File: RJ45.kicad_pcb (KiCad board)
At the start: 2 copper layers, 19.1 x 34.9 mm, 3 parts, among them J1 Conn_01x06, J2 RJ45_Amphenol_RJMG1BD3B8K1ANR, J3 Conn_01x06

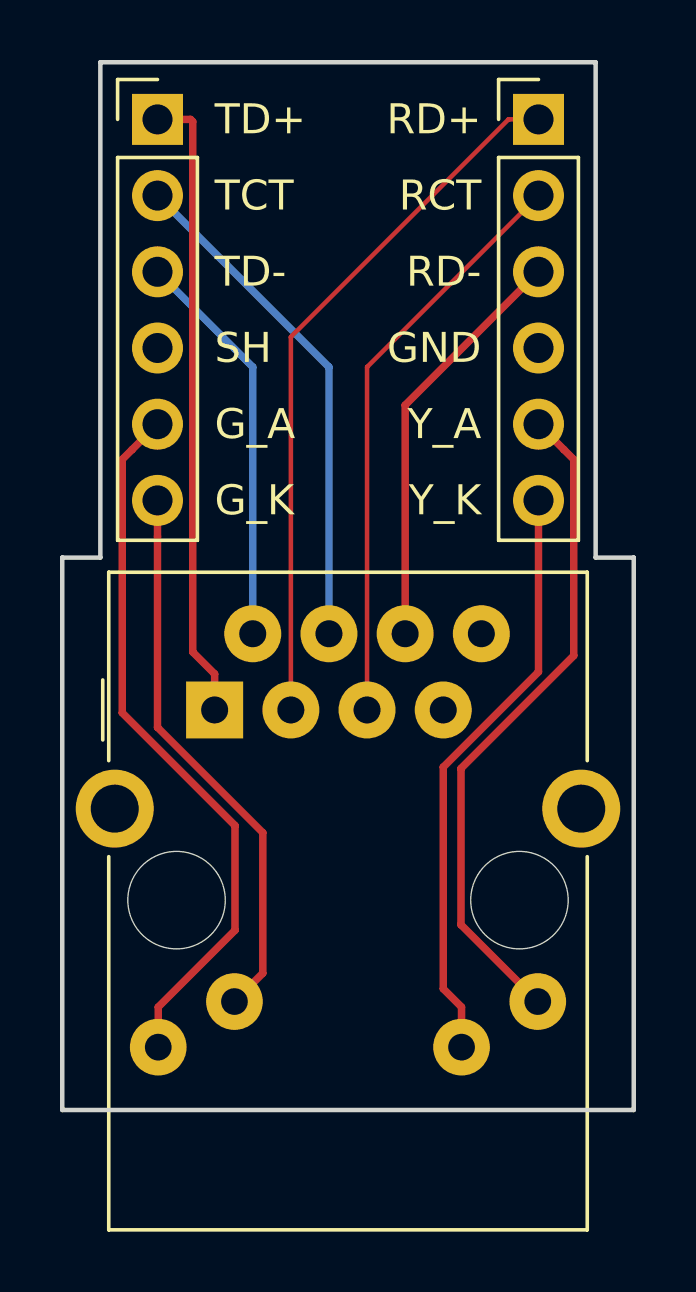
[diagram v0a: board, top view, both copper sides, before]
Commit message: Text on back silkscreen.
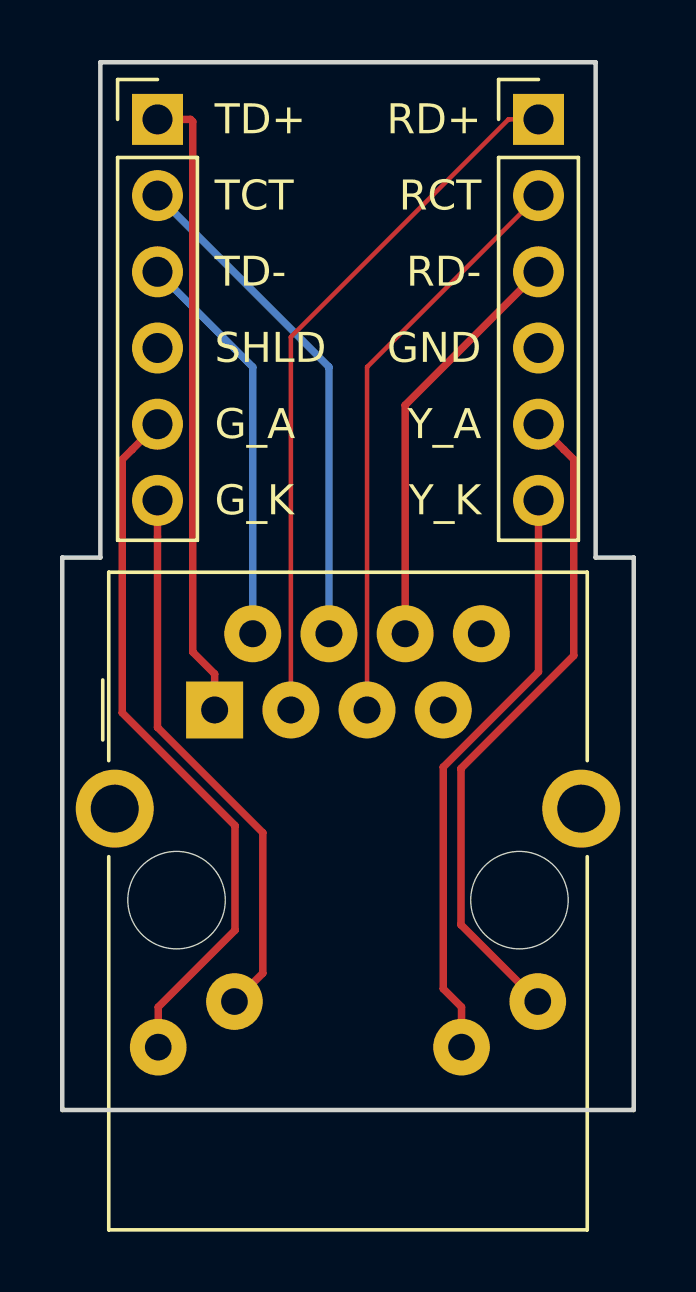
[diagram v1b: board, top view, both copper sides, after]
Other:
- board text added: "RJ45 Magjack Breakout 2018-04-24 Patrick Pelletier"
- board text added: "SHLD"
- board text removed: "SH"
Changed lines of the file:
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@@
     (area 0 0 0 0)
     (thickness 1.6)
-    (drawings 20)
+    (drawings 21)
     (tracks 39)
     (zones 0)
@@
   )
   (page USLetter)
+  (title_block
+    (title "RJ45 Magjack Breakout")
+    (date 2018-04-24)
+    (rev 1.0)
+    (company "Patrick Pelletier")
+  )
   (layers
     (0 F.Cu signal)
@@
     )
   )
+  (gr_text "RJ45\nMagjack\nBreakout\n2018-04-24\nPatrick\nPelletier" (at 138.43 83.82) (layer B.SilkS)
+    (effects (font (size 1 1) (thickness 0.2)) (justify mirror))
+  )
   (gr_text Y_K (at 142.875 90.17) (layer F.SilkS)
     (effects (font (size 1 1) (thickness 0.2)) (justify right))
@@
     (effects (font (size 1 1) (thickness 0.2)) (justify left))
   )
-  (gr_text SH (at 133.985 85.09) (layer F.SilkS)
+  (gr_text SHLD (at 133.985 85.09) (layer F.SilkS)
     (effects (font (size 1 1) (thickness 0.2)) (justify left))
   )
